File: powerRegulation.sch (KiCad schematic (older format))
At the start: 12 parts, among them U401 LM2931, U402 MCP1640T

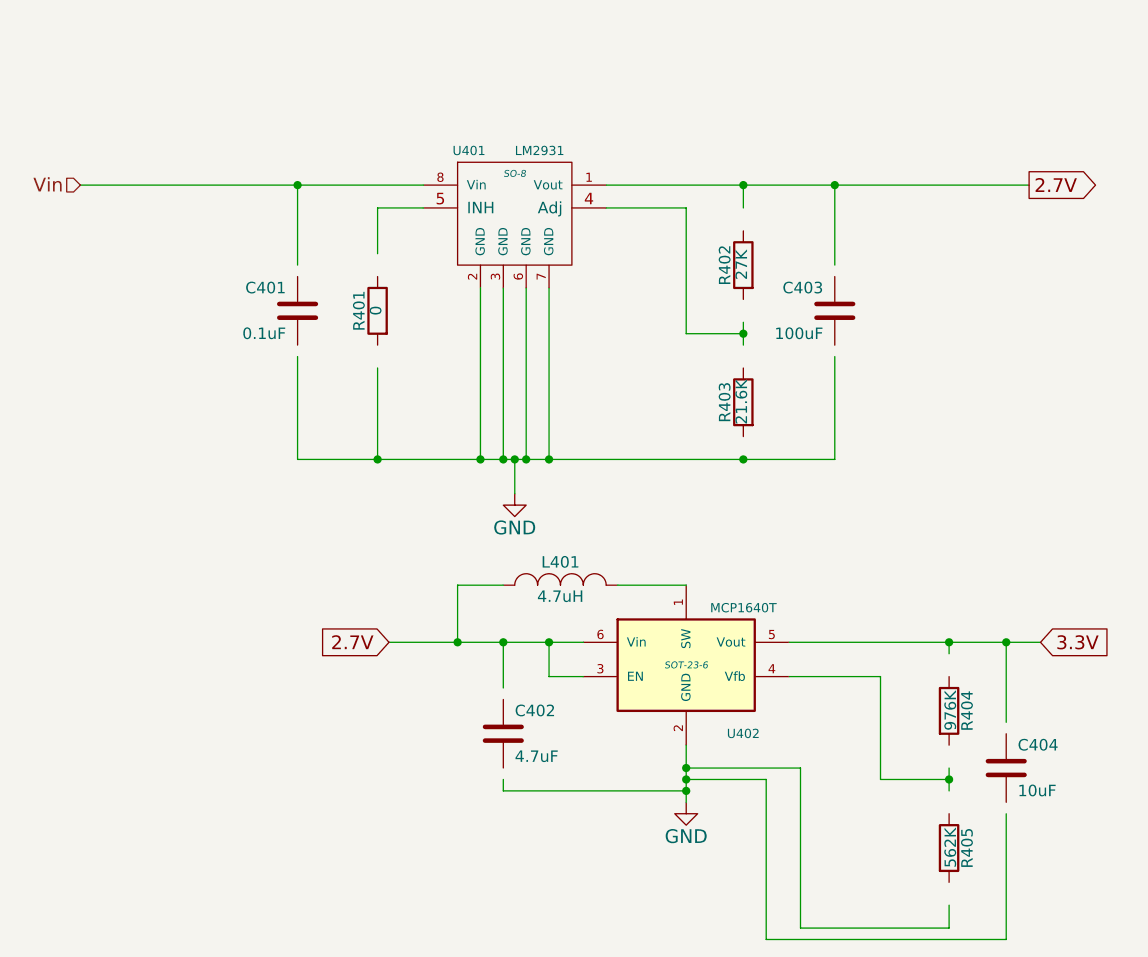
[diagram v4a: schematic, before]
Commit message: updated schematic with corrected wiring after all passives became disconnected
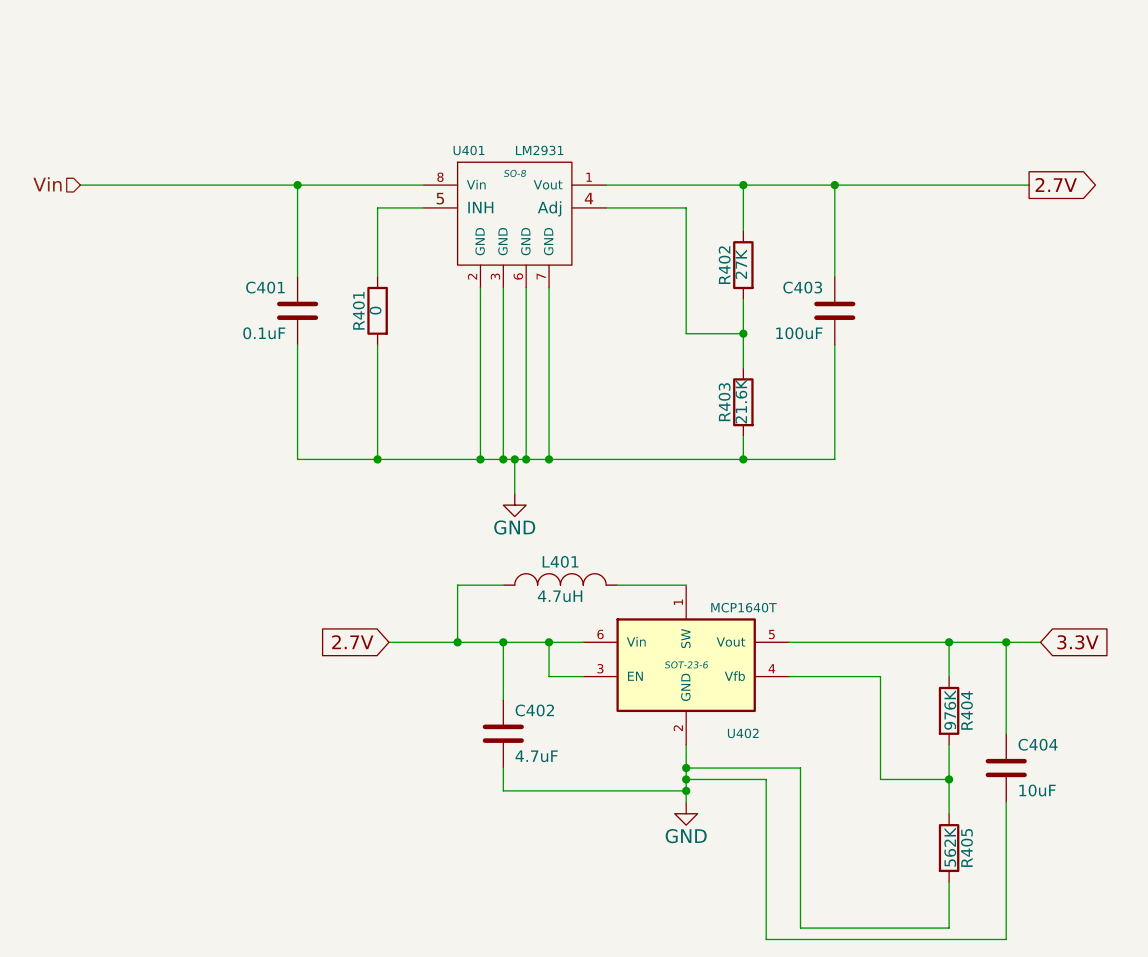
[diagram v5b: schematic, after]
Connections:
- wire segments 65 -> 46
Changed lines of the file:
@@
 Connection ~ 7200 2750
 Wire Wire Line
-	7200 2750 7200 3100
+	7200 2750 7200 3150
 Connection ~ 6800 2750
 Wire Wire Line
-	6800 2850 6800 2750
+	6800 2750 6800 2950
 Connection ~ 6800 3950
 Wire Wire Line
-	7200 3950 7200 3500
+	7200 3450 7200 3950
 Connection ~ 5200 3950
 Wire Wire Line
-	5200 3550 5200 3950
+	5200 3450 5200 3950
 Wire Wire Line
-	5200 2850 5200 3050
+	5200 2850 5200 3150
 Connection ~ 4850 2750
 Wire Wire Line
-	4850 3100 4850 2750
+	4850 2750 4850 3150
 Connection ~ 5650 3950
 Wire Wire Line
-	4850 3950 4850 3500
+	4850 3450 4850 3950
 Connection ~ 5750 3950
 Wire Wire Line
@@
 Connection ~ 5950 3950
 Wire Wire Line
-	5950 3200 5950 3950
+	5950 3950 5950 3200
 Connection ~ 5850 3950
 Wire Wire Line
-	5850 3200 5850 3950
+	5850 3950 5850 3200
 Wire Wire Line
 	5800 3950 5800 4100
 Wire Wire Line
-	4850 3950 5200 3950
-Wire Wire Line
-	5200 3950 5650 3950
-Wire Wire Line
-	5650 3950 5750 3950
-Wire Wire Line
-	5750 3950 5800 3950
-Wire Wire Line
-	5800 3950 5850 3950
-Wire Wire Line
-	5850 3950 5950 3950
-Wire Wire Line
-	5950 3950 6800 3950
-Wire Wire Line
-	6800 3950 7200 3950
+	4850 3950 7200 3950
 Connection ~ 6800 3400
 Wire Wire Line
@@
 	6550 2850 6550 3400
 Wire Wire Line
-	6800 3350 6800 3400
+	6800 3250 6800 3550
 Wire Wire Line
-	6800 3400 6800 3450
+	6200 2750 8050 2750
 Wire Wire Line
-	6200 2750 6800 2750
-Wire Wire Line
-	6800 2750 7200 2750
-Wire Wire Line
-	7200 2750 8050 2750
-Wire Wire Line
-	3900 2750 4850 2750
-Wire Wire Line
-	4850 2750 5400 2750
+	3900 2750 5400 2750
 Wire Wire Line
 	6250 4500 6550 4500
 Wire Wire Line
-	6550 5200 6550 5300
+	6550 5200 6550 5450
 Wire Wire Line
-	6550 5300 6550 5350
-Wire Wire Line
-	6550 5350 6550 5400
-Wire Wire Line
-	6550 5400 6550 5450
-Wire Wire Line
-	5250 4750 5550 4750
-Wire Wire Line
-	5550 4750 5750 4750
-Wire Wire Line
-	5750 4750 5950 4750
-Wire Wire Line
-	5950 4750 6100 4750
+	5250 4750 6100 4750
 Wire Wire Line
 	6100 4900 5950 4900
@@
 Connection ~ 5950 4750
 Wire Wire Line
-	5750 4950 5750 4750
+	5750 4750 5750 5000
 Connection ~ 5750 4750
 Wire Wire Line
-	5750 5350 5750 5400
+	5750 5300 5750 5400
 Wire Wire Line
 	5750 5400 6550 5400
@@
 Connection ~ 5550 4750
 Wire Wire Line
-	7000 4750 7700 4750
+	7000 4750 8100 4750
 Wire Wire Line
-	7700 4750 7950 4750
-Wire Wire Line
-	7950 4750 8100 4750
-Wire Wire Line
-	7700 4800 7700 4750
+	7700 4750 7700 4900
 Connection ~ 7700 4750
 Wire Wire Line
-	7700 5300 7700 5350
-Wire Wire Line
-	7700 5350 7700 5400
+	7700 5200 7700 5500
 Wire Wire Line
 	7000 4900 7400 4900
@@
 Connection ~ 7700 5350
 Wire Wire Line
-	7700 5900 7700 6000
+	7700 5800 7700 6000
 Wire Wire Line
 	7700 6000 7050 6000
@@
 Connection ~ 6550 5300
 Wire Wire Line
-	7950 5100 7950 4750
+	7950 4750 7950 5150
 Connection ~ 7950 4750
 Wire Wire Line
-	7950 5500 7950 6050
+	7950 5450 7950 6050
 Wire Wire Line
 	7950 6050 6900 6050
@@
 Wire Wire Line
 	6550 2850 6200 2850
+Wire Wire Line
+	6800 3850 6800 3950
 $EndSCHEMATC

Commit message: updated project with most footprint associations
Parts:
- added P401: TST, symbol TST
- C401, C402, C403, C404: footprint (none) -> Capacitors_SMD:C_0805_HandSoldering
- R401, R402, R403, R404, R405: footprint (none) -> Resistors_SMD:R_0805_HandSoldering
- U401: footprint SO-8 -> Power_Integrations:SO-8
- U402: footprint SOT-23-6 -> Housings_SOT-23_SOT-143_TSOT-6:SOT-23-6
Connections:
- net 2.7V: now also P401.1
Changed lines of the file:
@@
 $EndDescr
 $Comp
-L GND #PWR022
+L GND #PWR401
 U 1 1 5521C448
 P 5800 4100
-F 0 "#PWR022" H 5800 3850 60  0001 C CNN
+F 0 "#PWR401" H 5800 3850 60  0001 C CNN
 F 1 "GND" H 5800 3950 60  0000 C CNN
 F 2 "" H 5800 4100 60  0000 C CNN
@@
 F 0 "C401" H 4900 3400 50  0000 L CNN
 F 1 "0.1uF" H 4900 3200 50  0000 L CNN
-F 2 "" H 4888 3150 30  0000 C CNN
+F 2 "Capacitors_SMD:C_0805_HandSoldering" H 4888 3150 30  0001 C CNN
 F 3 "" H 4850 3300 60  0000 C CNN
 	1    4850 3300
@@
 F 0 "C403" H 7250 3400 50  0000 L CNN
 F 1 "100uF" H 7250 3200 50  0000 L CNN
-F 2 "" H 7238 3150 30  0000 C CNN
+F 2 "Capacitors_SMD:C_0805_HandSoldering" H 7238 3150 30  0001 C CNN
 F 3 "" H 7200 3300 60  0000 C CNN
 	1    7200 3300
@@
 F 0 "R402" V 6880 3100 50  0000 C CNN
 F 1 "27K" V 6807 3101 50  0000 C CNN
-F 2 "" V 6730 3100 30  0000 C CNN
+F 2 "Resistors_SMD:R_0805_HandSoldering" V 6730 3100 30  0001 C CNN
 F 3 "" H 6800 3100 30  0000 C CNN
 	1    6800 3100
@@
 F 0 "R403" V 6880 3700 50  0000 C CNN
 F 1 "21.6K" V 6807 3701 50  0000 C CNN
-F 2 "" V 6730 3700 30  0000 C CNN
+F 2 "Resistors_SMD:R_0805_HandSoldering" V 6730 3700 30  0001 C CNN
 F 3 "" H 6800 3700 30  0000 C CNN
 	1    6800 3700
@@
 F 0 "R401" V 5280 3300 50  0000 C CNN
 F 1 "0" V 5207 3301 50  0000 C CNN
-F 2 "" V 5130 3300 30  0000 C CNN
+F 2 "Resistors_SMD:R_0805_HandSoldering" V 5130 3300 30  0001 C CNN
 F 3 "" H 5200 3300 30  0000 C CNN
 	1    5200 3300
@@
 F 0 "U402" H 6800 4650 40  0000 C CNN
 F 1 "MCP1640T" H 6800 5200 40  0000 C CNN
-F 2 "SOT-23-6" H 6550 4950 30  0000 C CIN
+F 2 "Housings_SOT-23_SOT-143_TSOT-6:SOT-23-6" H 6550 4950 30  0000 C CIN
 F 3 "" H 6550 4900 60  0000 C CNN
 	1    6550 4900
@@
 F 0 "L401" H 6000 4600 50  0000 C CNN
 F 1 "4.7uH" H 6000 4450 50  0000 C CNN
-F 2 "" H 6000 4500 60  0000 C CNN
+F 2 "" H 6000 4500 60  0001 C CNN
 F 3 "" H 6000 4500 60  0000 C CNN
 F 4 "Value" H 6000 4500 60  0001 C CNN "MPN"
@@
 $EndComp
 $Comp
-L GND #PWR023
+L GND #PWR402
 U 1 1 55228946
 P 6550 5450
-F 0 "#PWR023" H 6550 5200 60  0001 C CNN
+F 0 "#PWR402" H 6550 5200 60  0001 C CNN
 F 1 "GND" H 6550 5300 60  0000 C CNN
 F 2 "" H 6550 5450 60  0000 C CNN
@@
 F 0 "C402" H 5800 5250 50  0000 L CNN
 F 1 "4.7uF" H 5800 5050 50  0000 L CNN
-F 2 "" H 5788 5000 30  0000 C CNN
+F 2 "Capacitors_SMD:C_0805_HandSoldering" H 5788 5000 30  0001 C CNN
 F 3 "" H 5750 5150 60  0000 C CNN
 F 4 "Value" H 5750 5150 60  0001 C CNN "MPN"
@@
 F 0 "R404" V 7780 5050 50  0000 C CNN
 F 1 "976K" V 7707 5051 50  0000 C CNN
-F 2 "" V 7630 5050 30  0000 C CNN
+F 2 "Resistors_SMD:R_0805_HandSoldering" V 7630 5050 30  0001 C CNN
 F 3 "" H 7700 5050 30  0000 C CNN
 	1    7700 5050
@@
 F 0 "R405" V 7780 5650 50  0000 C CNN
 F 1 "562K" V 7707 5651 50  0000 C CNN
-F 2 "" V 7630 5650 30  0000 C CNN
+F 2 "Resistors_SMD:R_0805_HandSoldering" V 7630 5650 30  0001 C CNN
 F 3 "" H 7700 5650 30  0000 C CNN
 	1    7700 5650
@@
 F 0 "C404" H 8000 5400 50  0000 L CNN
 F 1 "10uF" H 8000 5200 50  0000 L CNN
-F 2 "" H 7988 5150 30  0000 C CNN
+F 2 "Capacitors_SMD:C_0805_HandSoldering" H 7988 5150 30  0001 C CNN
 F 3 "" H 7950 5300 60  0000 C CNN
 	1    7950 5300
@@
 F 0 "U401" H 5600 3000 40  0000 C CNN
 F 1 "LM2931" H 5800 3000 40  0000 L CNN
-F 2 "SO-8" H 5800 2900 30  0000 C CIN
+F 2 "Power_Integrations:SO-8" H 5800 2900 30  0000 C CIN
 F 3 "" H 5800 2700 60  0000 C CNN
 	1    5800 2800
@@
 Wire Wire Line
 	6800 3850 6800 3950
+$Comp
+L TST P401
+U 1 1 5528ED00
+P 7550 2400
+F 0 "P401" H 7550 2700 50  0000 C BNN
+F 1 "TST" H 7550 2650 50  0000 C CNN
+F 2 "" H 7550 2400 60  0000 C CNN
+F 3 "" H 7550 2400 60  0000 C CNN
+	1    7550 2400
+	1    0    0    -1
+$EndComp
+Wire Wire Line
+	7550 2400 7550 2750
+Connection ~ 7550 2750
 $EndSCHEMATC

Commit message: association of footprints complete
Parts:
- L401: footprint (none) -> Resistors_SMD:R_0805_HandSoldering; MPN Value -> AIML-0805HC-4R7M-T
- P401: footprint (none) -> Measurement_Points:Measurement_Point_Round-TH_Small
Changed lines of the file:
@@
 $EndDescr
 $Comp
-L GND #PWR401
+L GND #PWR022
 U 1 1 5521C448
 P 5800 4100
-F 0 "#PWR401" H 5800 3850 60  0001 C CNN
+F 0 "#PWR022" H 5800 3850 60  0001 C CNN
 F 1 "GND" H 5800 3950 60  0000 C CNN
 F 2 "" H 5800 4100 60  0000 C CNN
@@
 F 0 "L401" H 6000 4600 50  0000 C CNN
 F 1 "4.7uH" H 6000 4450 50  0000 C CNN
-F 2 "" H 6000 4500 60  0001 C CNN
-F 3 "" H 6000 4500 60  0000 C CNN
-F 4 "Value" H 6000 4500 60  0001 C CNN "MPN"
+F 2 "Resistors_SMD:R_0805_HandSoldering" H 6000 4500 60  0001 C CNN
+F 3 "http://www.abracon.com/Magnetics/inductors/AIML-0805HC.pdf" H 6000 4500 60  0001 C CNN
+F 4 "AIML-0805HC-4R7M-T" H 6000 4500 60  0001 C CNN "MPN"
 	1    6000 4500
 	1    0    0    -1
 $EndComp
 $Comp
-L GND #PWR402
+L GND #PWR023
 U 1 1 55228946
 P 6550 5450
-F 0 "#PWR402" H 6550 5200 60  0001 C CNN
+F 0 "#PWR023" H 6550 5200 60  0001 C CNN
 F 1 "GND" H 6550 5300 60  0000 C CNN
 F 2 "" H 6550 5450 60  0000 C CNN
@@
 F 0 "P401" H 7550 2700 50  0000 C BNN
 F 1 "TST" H 7550 2650 50  0000 C CNN
-F 2 "" H 7550 2400 60  0000 C CNN
+F 2 "Measurement_Points:Measurement_Point_Round-TH_Small" H 7550 2400 60  0001 C CNN
 F 3 "" H 7550 2400 60  0000 C CNN
 	1    7550 2400
